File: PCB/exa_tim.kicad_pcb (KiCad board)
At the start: 4 copper layers, 42 x 42 mm, 52 parts, among them J1 20021112-00010T4LF, J2 FH12-24S-0.5SH(55), Q1 SI2333DS-T1-E3, Q2 DMN3067LW-7, SW1 TL3305CF260QG, SW2 TL3305CF260QG, SW3 TL3305CF260QG, SW4 TL3305CF260QG, U1 STM32L071KZUx, U2 CAM-M8C-0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

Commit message: Rework ground and power plane
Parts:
- moved C13 0.28 mm to (118.5, 95.2), turned to 0 degrees
- moved Q2 0.15 mm to (120.6, 98.3)
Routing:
- net GND: track 37.8 -> 92.9 mm, vias 19 -> 36
- net 3V: track 98.7 -> 94.9 mm, vias 11 -> 12
- net /SWDIO: track 23.9 -> 26.0 mm
- net /BUSY: track 24.7 -> 23.2 mm
- net /CS: track 20.7 -> 21.8 mm
- net /BTN2: track 47.9 -> 48.8 mm
- net /WKUP1: track 114.8 -> 115.6 mm
- net /BTN1: track 41.3 -> 42.0 mm
- net /SWCLK: track 28.4 -> 27.7 mm
- removed copper zone on F.Cu, net GND

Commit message: Add message that only precious few will understand
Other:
- board text added: "DC 180831"
- board text added: "EX[cieran & linc-ala];"
- board text added: "ih=yen-yela soh-nh syen-sey-la;"
- board text added: "lolosy tiria etolu tisia"
- board text removed: "DC 180830"
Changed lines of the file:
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@@
   (general
     (thickness 1)
-    (drawings 24)
+    (drawings 27)
     (tracks 595)
     (zones 0)
@@
     (tags "Keystone type 3034 coin cell retainer")
     (attr smd)
-    (fp_text reference BT1 (at 0 11.5 180) (layer B.SilkS)
+    (fp_text reference BT1 (at 0 11.2 180) (layer B.SilkS)
       (effects (font (size 1 1) (thickness 0.15)) (justify mirror))
     )
@@
     )
   )
+  (gr_text "lolosy tiria etolu tisia" (at 120.9 110.725) (layer B.SilkS)
+    (effects (font (size 1 1) (thickness 0.15)) (justify mirror))
+  )
+  (gr_text "EX[cieran & linc-ala];" (at 120.75 109.175) (layer B.SilkS)
+    (effects (font (size 1 1) (thickness 0.15)) (justify mirror))
+  )
+  (gr_text "ih=yen-yela soh-nh syen-sey-la;" (at 120.475 107.5) (layer B.SilkS)
+    (effects (font (size 1 1) (thickness 0.15)) (justify mirror))
+  )
   (gr_line (start 142 103.6) (end 142 78.4) (layer Edge.Cuts) (width 0.15))
   (gr_line (start 142 107) (end 142 103.6) (layer Edge.Cuts) (width 0.15))
@@
     (effects (font (size 1 1) (thickness 0.15)))
   )
-  (gr_text "DC 180830" (at 132.3 73.6) (layer F.SilkS)
+  (gr_text "DC 180831" (at 132.3 73.6) (layer F.SilkS)
     (effects (font (size 1 1) (thickness 0.15)))
   )

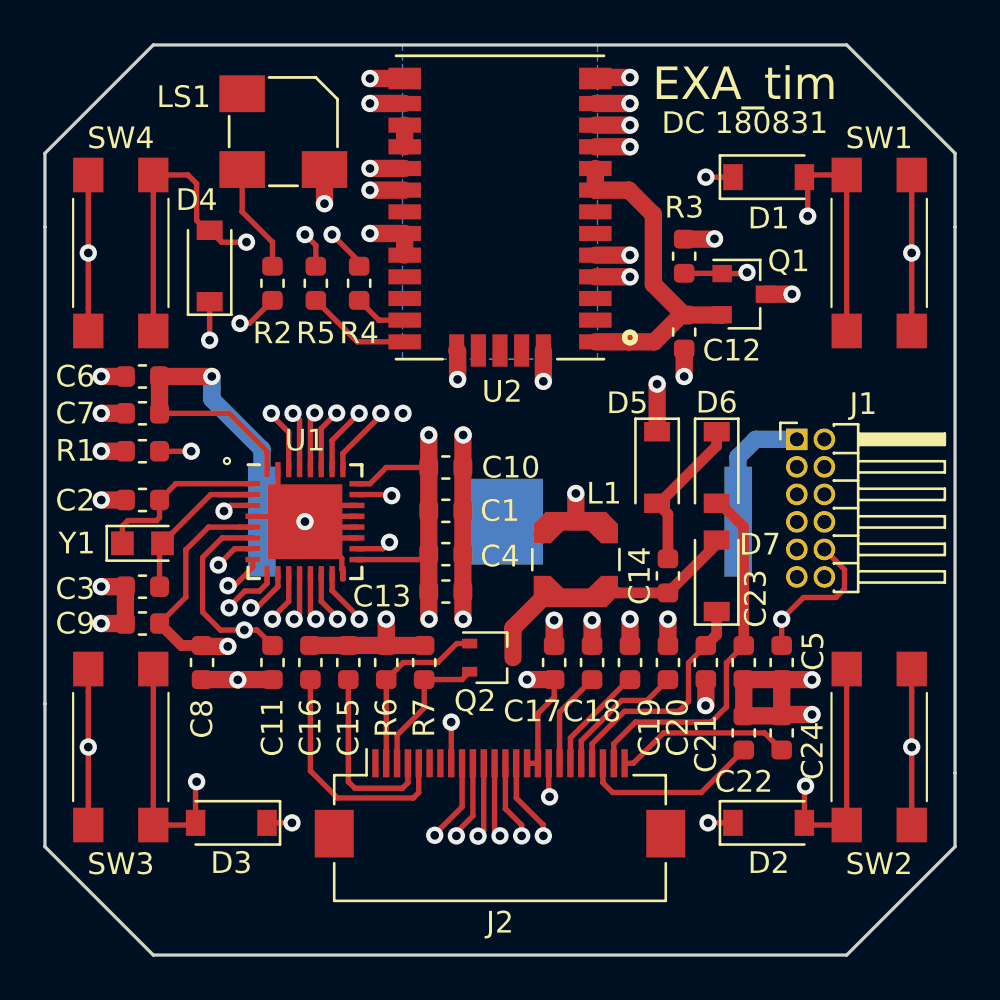
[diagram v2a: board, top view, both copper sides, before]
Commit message: Rework power plane and GND of STM32L0 chip
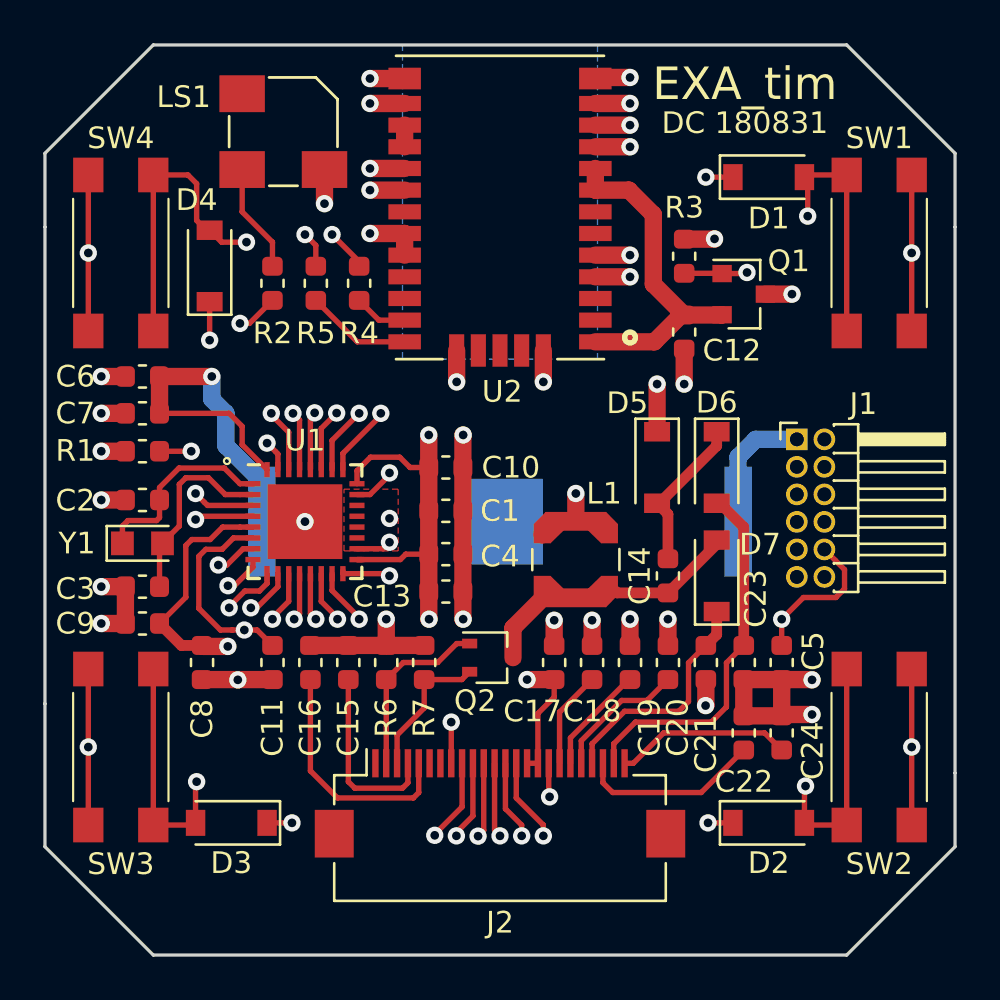
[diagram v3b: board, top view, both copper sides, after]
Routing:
- net GND: track 92.9 -> 85.6 mm, vias 36 -> 40
- net /SWDIO: track 26.0 -> 23.8 mm, vias 2 -> 1
- net /BTN1: track 42.0 -> 40.1 mm
- net /NRST: track 38.2 -> 39.2 mm
- net Net-(C2-Pad1): track 8.40 -> 9.33 mm
- net /BTN2: track 48.8 -> 49.7 mm
- net 3V: track 94.9 -> 95.7 mm
- net /BTN3: track 35.1 -> 35.9 mm
- net /GNSS_EN: track 34.5 -> 35.2 mm
- net /SWCLK: track 27.7 -> 27.1 mm
- added copper zone on F.Cu, net GND

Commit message: Change crystal caps from 21 to 20pF
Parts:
- C2, C3: value 21pF -> 20pF
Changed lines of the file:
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@@
       (effects (font (size 1 1) (thickness 0.15)))
     )
-    (fp_text value 21pF (at 0 1.43 180) (layer F.Fab)
+    (fp_text value 20pF (at 0 1.43 180) (layer F.Fab)
       (effects (font (size 1 1) (thickness 0.15)))
     )
@@
       (effects (font (size 1 1) (thickness 0.15)))
     )
-    (fp_text value 21pF (at 0 1.43 180) (layer F.Fab)
+    (fp_text value 20pF (at 0 1.43 180) (layer F.Fab)
       (effects (font (size 1 1) (thickness 0.15)))
     )
